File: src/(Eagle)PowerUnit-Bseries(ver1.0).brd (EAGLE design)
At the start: 100 x 100 mm, 88 parts, among them CON1 XT90PW-M, CON2 XT90PW-F, CON3 XT60PW-F, CON4 XT60PW-F, CON5 XT60PW-F, CON6 XT60PW-F, Q1 DMP3056L-7, Q2 DMP3056L-7, Q3 DMP3056L-7, U1 LQFP64, U2 MCP2517FD, U3 CH340E, U4 AP63203WU-7, U5 AP63205WU-7, U6 AP331AWG-7, U7 AP331AWG-7, U8 AP331AWG-7

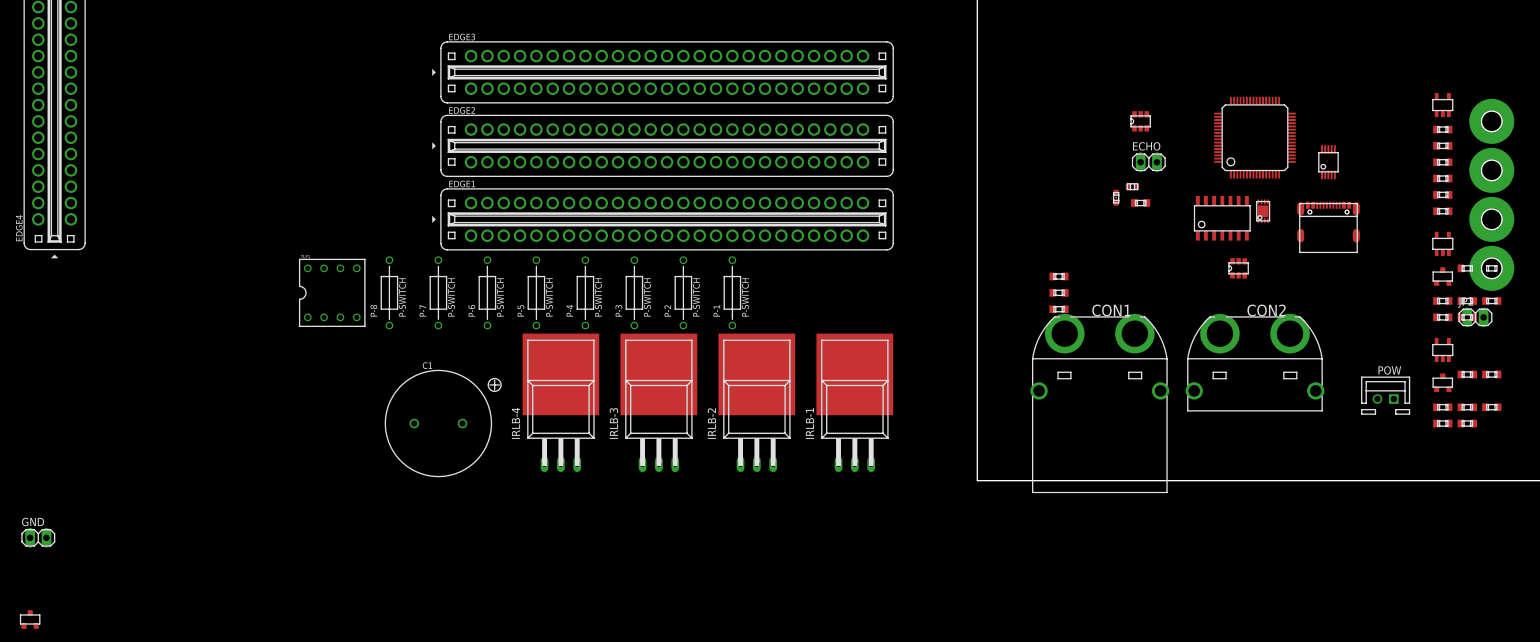
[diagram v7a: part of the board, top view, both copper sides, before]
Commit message: 5VDCDCのMLCC選定、電源回りの整理
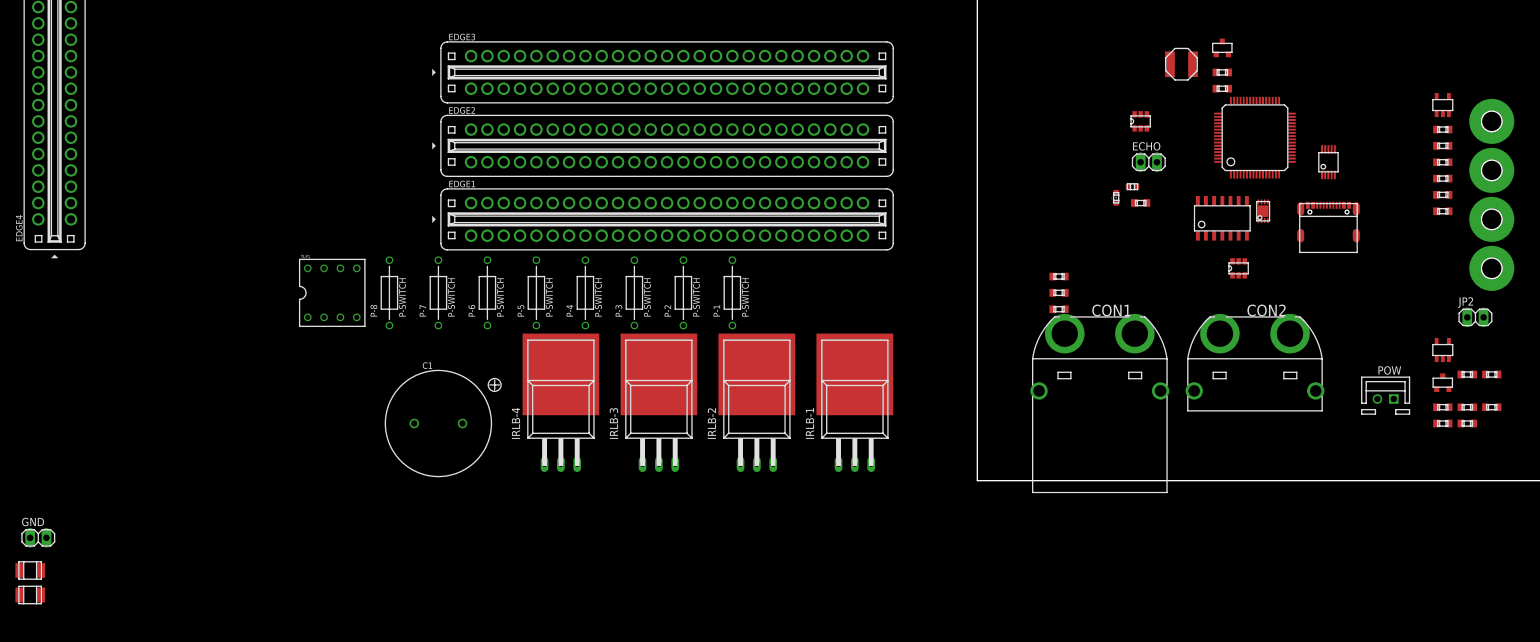
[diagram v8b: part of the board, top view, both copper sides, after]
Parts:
- removed Q2: DMP3056L-7, DMP3056L-7:SOT23
- removed R20, R21, R22: 10k, CR0603:CR0603
- removed R23: 100k, CR0603:CR0603
- removed R24: 0, CR0603:CR0603
- removed U7: AP331AWG-7, AP331AWG-7:SOT25
- added C4, C5: GRM32ER71H106KA12, GRM32ER71H106KA12:GRM32ER71H106KA12
- added L1: 4.7uH, NRS5030T4R7MMGJ:NRS5030T4R7MMGJ
- R18: value 10k -> 0
- R19: value 10k -> ∞
- moved Q1 205.6 mm to (38.1, 67.3)
- moved R19 50.4 mm to (38.1, 61.0)
- moved R18 48.8 mm to (38.1, 63.5)
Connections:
- removed net N$41: Q2.G, R18.RIGHT, R23.LEFT, R24.LEFT, R24.RIGHT, U7.OUTPUT
- removed net N$43: R19.LEFT, R20.RIGHT, U7.IN-
- removed net N$44: R21.LEFT, R22.RIGHT, U7.IN+
- new net N$36: R18.LEFT, R19.RIGHT, U5.EN
- new net N$40: L1.L, U5.SW
- net GND2: now also C4.R, C5.R, R19.LEFT; no longer R20.LEFT, R22.LEFT, U7.GND
- net U5V: no longer Q2.D, R19.RIGHT
- net V+: now also C4.L, C5.L, R18.RIGHT, U5.VIN; no longer Q2.S, R18.LEFT, R21.RIGHT, R23.RIGHT, U7.VCC
